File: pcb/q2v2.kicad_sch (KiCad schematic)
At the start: 13 parts, among them J1 USB_B

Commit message: Pi programmer.
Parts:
- removed D1: Blue, LED_SMD:LED_0805_2012Metric, symbol Device:LED
- removed R1: 4.7k, Resistor_SMD:R_0805_2012Metric, symbol Device:R
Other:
- added sheet Programmer (programmer.kicad_sch)

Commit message: Bit low/high.
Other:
- sheet Bit 0: file bit.kicad_sch -> bit-low.kicad_sch
- sheet Bit 1: file bit.kicad_sch -> bit-low.kicad_sch
- sheet Bit 10: file bit.kicad_sch -> bit-high.kicad_sch
- sheet Bit 11: file bit.kicad_sch -> bit-high.kicad_sch
- sheet Bit 2: file bit.kicad_sch -> bit-low.kicad_sch
- sheet Bit 3: file bit.kicad_sch -> bit-low.kicad_sch
- sheet Bit 4: file bit.kicad_sch -> bit-low.kicad_sch
- sheet Bit 7: file bit.kicad_sch -> bit-high.kicad_sch
- sheet Bit 8: file bit.kicad_sch -> bit-high.kicad_sch
- sheet Bit 9: file bit.kicad_sch -> bit-high.kicad_sch
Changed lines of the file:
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@@
       (effects (font (size 1.27 1.27)) (justify left bottom))
     )
-    (property "Sheet file" "bit.kicad_sch" (id 1) (at 318.77 136.3985 0)
+    (property "Sheet file" "bit-low.kicad_sch" (id 1) (at 318.77 136.399 0)
       (effects (font (size 1.27 1.27)) (justify left top))
     )
@@
       (effects (font (size 1.27 1.27)) (justify left bottom))
     )
-    (property "Sheet file" "bit.kicad_sch" (id 1) (at 266.7 136.3985 0)
+    (property "Sheet file" "bit-low.kicad_sch" (id 1) (at 266.7 136.399 0)
       (effects (font (size 1.27 1.27)) (justify left top))
     )
@@
       (effects (font (size 1.27 1.27)) (justify left bottom))
     )
-    (property "Sheet file" "bit.kicad_sch" (id 1) (at 114.3 76.7085 0)
+    (property "Sheet file" "bit-high.kicad_sch" (id 1) (at 114.3 76.709 0)
       (effects (font (size 1.27 1.27)) (justify left top))
     )
@@
       (effects (font (size 1.27 1.27)) (justify left bottom))
     )
-    (property "Sheet file" "bit.kicad_sch" (id 1) (at 59.69 76.7085 0)
+    (property "Sheet file" "bit-high.kicad_sch" (id 1) (at 59.69 76.709 0)
       (effects (font (size 1.27 1.27)) (justify left top))
     )
@@
       (effects (font (size 1.27 1.27)) (justify left bottom))
     )
-    (property "Sheet file" "bit.kicad_sch" (id 1) (at 215.9 136.3985 0)
+    (property "Sheet file" "bit-low.kicad_sch" (id 1) (at 215.9 136.399 0)
       (effects (font (size 1.27 1.27)) (justify left top))
     )
@@
       (effects (font (size 1.27 1.27)) (justify left bottom))
     )
-    (property "Sheet file" "bit.kicad_sch" (id 1) (at 165.1 136.3985 0)
+    (property "Sheet file" "bit-low.kicad_sch" (id 1) (at 165.1 136.399 0)
       (effects (font (size 1.27 1.27)) (justify left top))
     )
@@
       (effects (font (size 1.27 1.27)) (justify left bottom))
     )
-    (property "Sheet file" "bit.kicad_sch" (id 1) (at 114.3 136.3985 0)
+    (property "Sheet file" "bit-low.kicad_sch" (id 1) (at 114.3 136.399 0)
       (effects (font (size 1.27 1.27)) (justify left top))
     )
@@
       (effects (font (size 1.27 1.27)) (justify left bottom))
     )
-    (property "Sheet file" "bit.kicad_sch" (id 1) (at 266.7 76.7085 0)
+    (property "Sheet file" "bit-high.kicad_sch" (id 1) (at 266.7 76.709 0)
       (effects (font (size 1.27 1.27)) (justify left top))
     )
@@
       (effects (font (size 1.27 1.27)) (justify left bottom))
     )
-    (property "Sheet file" "bit.kicad_sch" (id 1) (at 215.9 76.7085 0)
+    (property "Sheet file" "bit-high.kicad_sch" (id 1) (at 215.9 76.709 0)
       (effects (font (size 1.27 1.27)) (justify left top))
     )
@@
       (effects (font (size 1.27 1.27)) (justify left bottom))
     )
-    (property "Sheet file" "bit.kicad_sch" (id 1) (at 165.1 76.7085 0)
-      (effects (font (size 1.27 1.27)) (justify left top))
-    )
+    (property "Sheet file" "bit-high.kicad_sch" (id 1) (at 165.1 76.709 0)
+      (effects (font (size 1.27 1.27)) (justify left top))
+    )

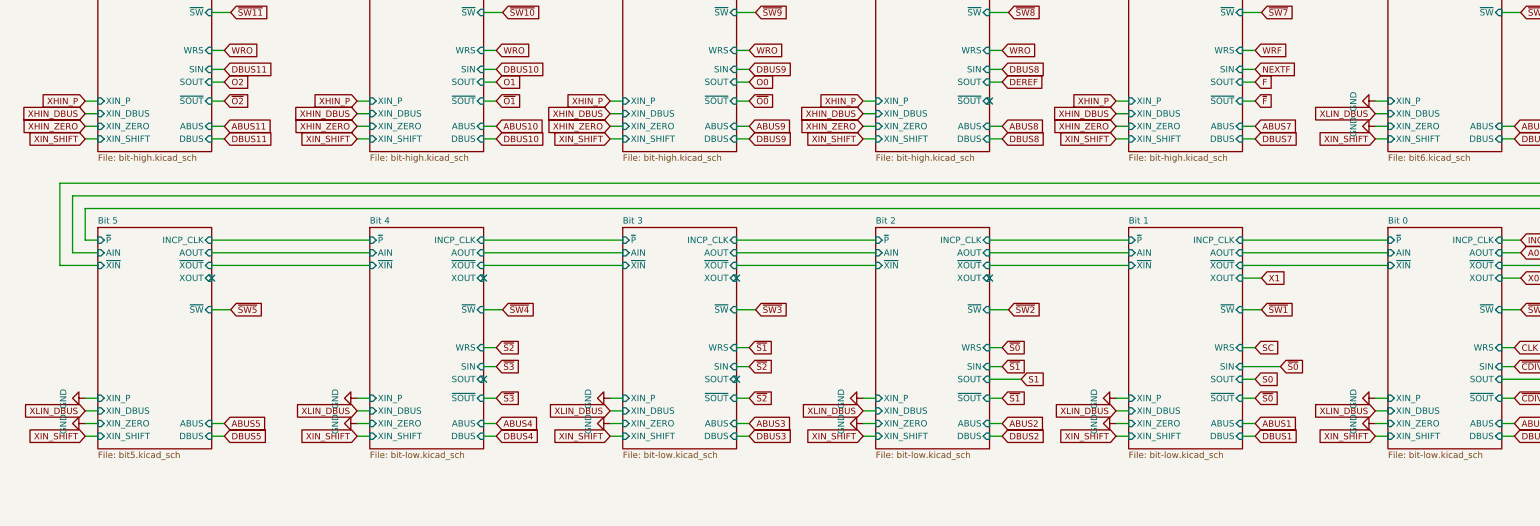
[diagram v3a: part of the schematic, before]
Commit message: Fewer transistors.
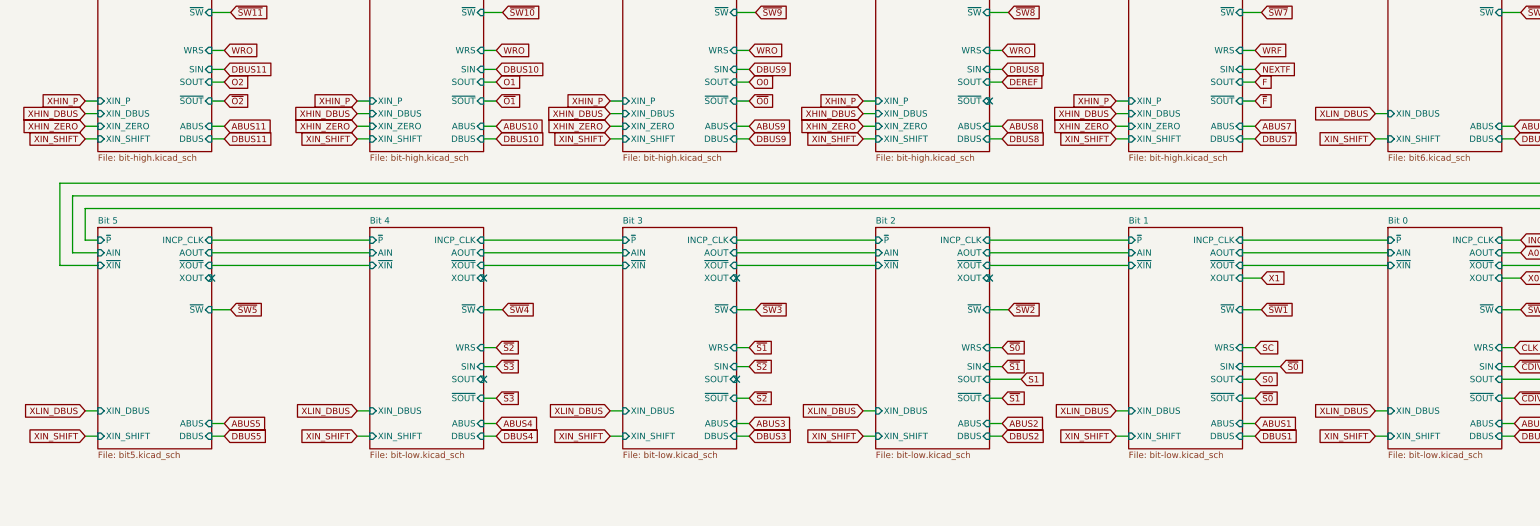
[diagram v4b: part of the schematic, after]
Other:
- sheet Bit 0 ports: added none; removed XIN_P, XIN_ZERO
- sheet Bit 1 ports: added none; removed XIN_P, XIN_ZERO
- sheet Bit 2 ports: added none; removed XIN_P, XIN_ZERO
- sheet Bit 3 ports: added none; removed XIN_P, XIN_ZERO
- sheet Bit 4 ports: added none; removed XIN_P, XIN_ZERO
- sheet Bit 5 ports: added none; removed XIN_P, XIN_ZERO
- sheet Bit 6 ports: added none; removed XIN_P, XIN_ZERO

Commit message: New reset.
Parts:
- C1, C2, C3, C4: value 0.47u -> 1u; LCSC C13967 -> C28323

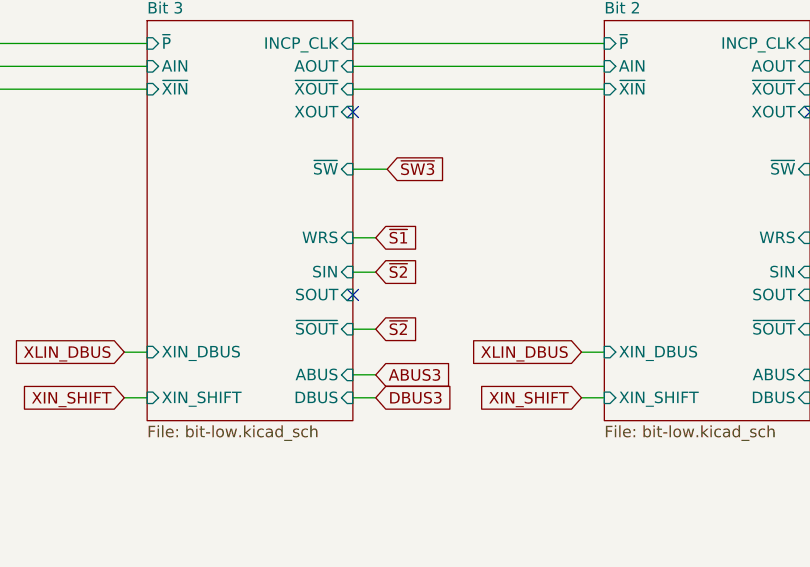
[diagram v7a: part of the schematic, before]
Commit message: Skip ALU state for jfc/jmp/sta.
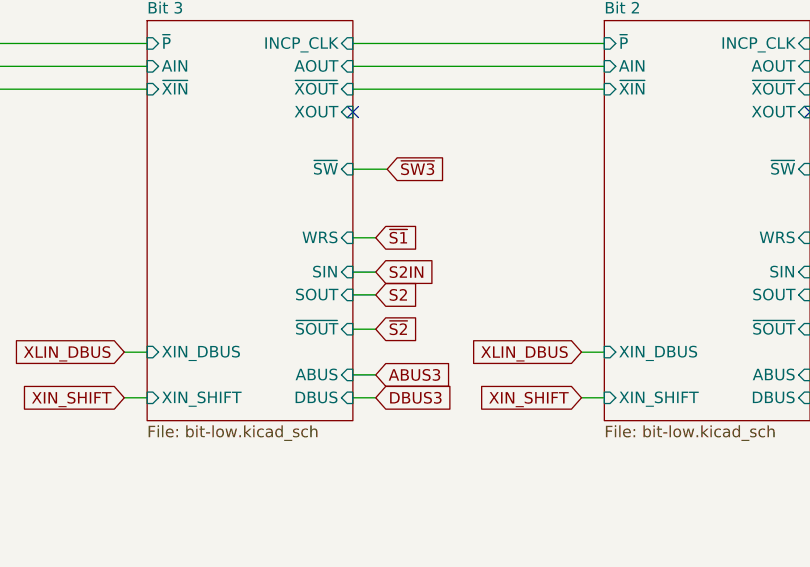
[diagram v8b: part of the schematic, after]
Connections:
- no-connect marks 16 -> 15
